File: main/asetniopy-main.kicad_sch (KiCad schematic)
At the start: 20 parts, among them J1 Conn_01x02, J2 Conn_01x02, J3 Conn_01x02, J4 Conn_01x02, J5 Conn_01x02, J6 Power/Reset, J7 BAT+, J8 BAT-, U1 ProMicro, U2 LSM6DSO

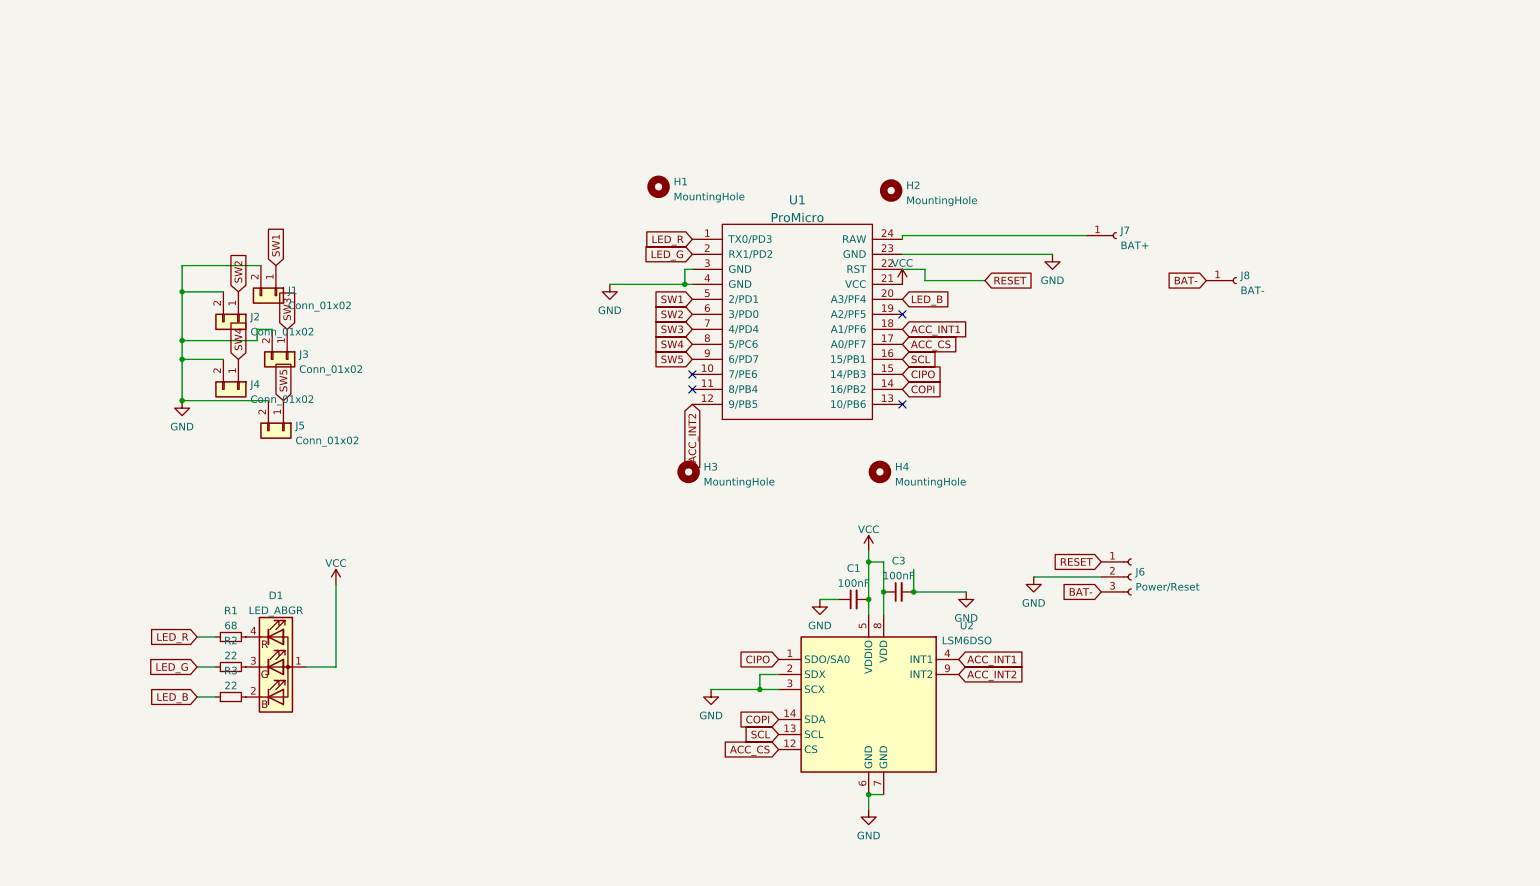
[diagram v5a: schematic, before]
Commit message: Left and right boards, joined via mouse bites.
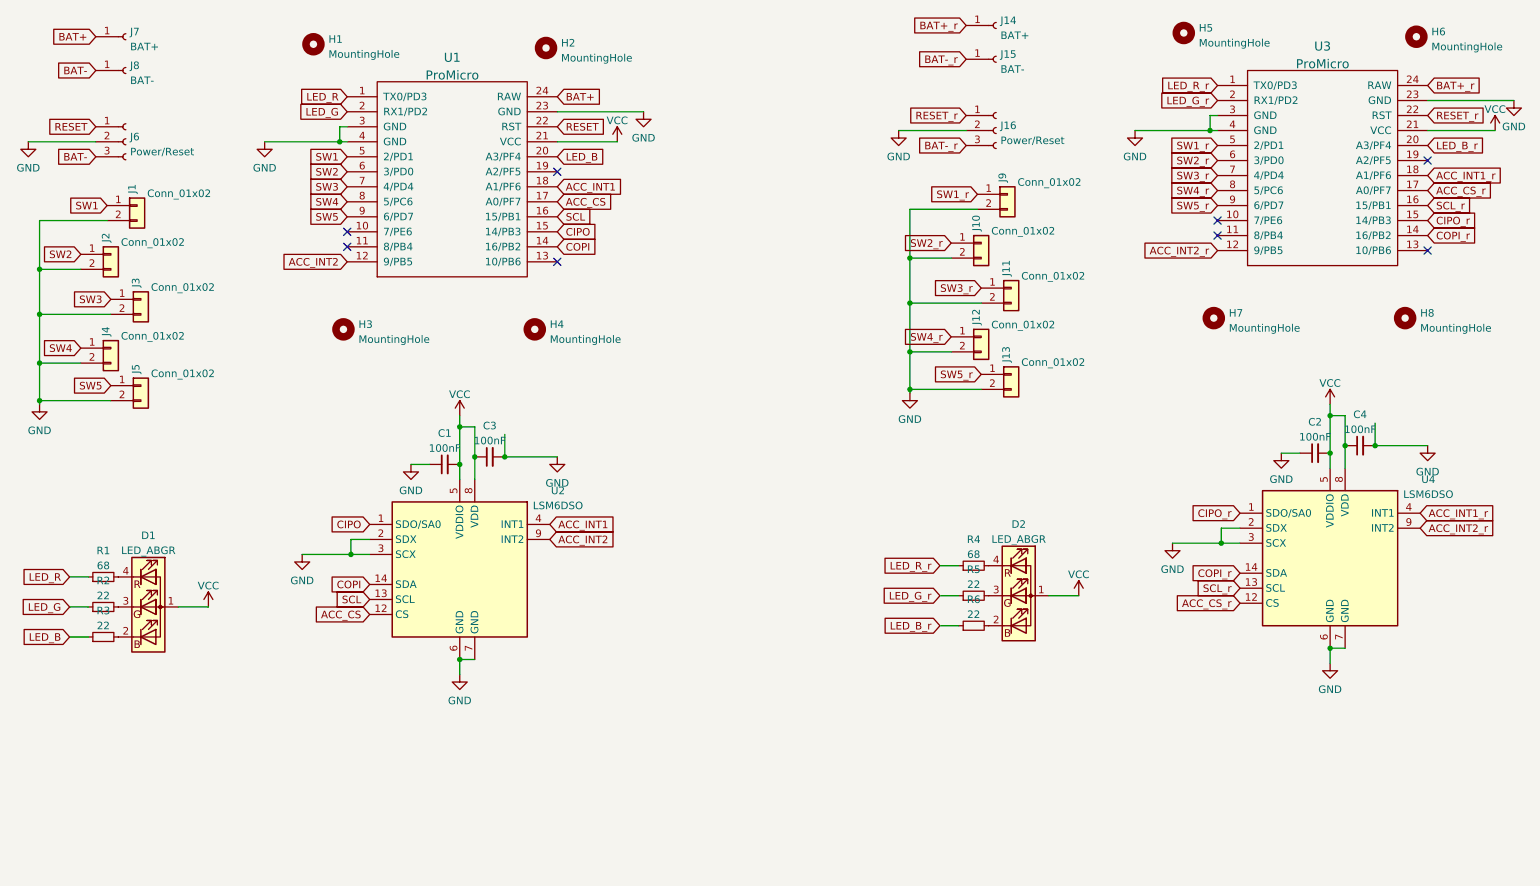
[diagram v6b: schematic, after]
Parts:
- added C2, C4: 100nF, Capacitor_SMD:C_0603_1608Metric, symbol Device:C_Small
- added D2: LED_ABGR, LED_SMD:LED_RGB_Wuerth-PLCC4_3.2x2.8mm_150141M173100, symbol Device:LED_ABGR
- added H5, H6, H7, H8: MountingHole, MountingHole:MountingHole_2.2mm_M2_Pad, symbol Mechanical:MountingHole
- added J10, J11, J12, J13, J9: Conn_01x02, Connector_Molex:Molex_Pico-EZmate_78171-0002_1x02-1MP_P1.20mm_Vertical, symbol Connector_Generic:Conn_01x02
- added J14: BAT+, Connector_PinSocket_2.54mm:PinSocket_1x01_P2.54mm_Vertical, symbol Connector:Conn_01x01_Female
- added J15: BAT-, Connector_PinSocket_2.54mm:PinSocket_1x01_P2.54mm_Vertical, symbol Connector:Conn_01x01_Female
- added J16: Power/Reset, Connector_Molex:Molex_Pico-EZmate_78171-0003_1x03-1MP_P1.20mm_Vertical, symbol Connector:Conn_01x03_Female
- added R4: 68, Resistor_SMD:R_0603_1608Metric, symbol Device:R_Small
- added R5, R6: 22, Resistor_SMD:R_0603_1608Metric, symbol Device:R_Small
- added U3: ProMicro, Keebio-Parts:ArduinoProMicro, symbol keebio:ProMicro
- added U4: LSM6DSO, main:PQFN50P250X300X86-14N, symbol Sensor_Motion:LSM6DS3
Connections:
- net BAT+: now reaches J7.1 (Pin_1), U1.24 (RAW)
- new net: D2.3 (GK), R5.2
- new net: D2.4 (RK), R4.2
- new net: D2.2 (BK), R6.2
- new net ACC_CS_r: U3.17 (A0/PF7), U4.12 (CS)
- new net ACC_INT1_r: U3.18 (A1/PF6), U4.4 (INT1)
- new net ACC_INT2_r: U3.12 (9/PB5), U4.9 (INT2)
- new net BAT+_r: J14.1 (Pin_1), U3.24 (RAW)
- new net BAT-_r: J15.1 (Pin_1), J16.3 (Pin_3)
- new net CIPO_r: U3.15 (14/PB3), U4.1 (SDO/SA0)
- new net COPI_r: U3.14 (16/PB2), U4.14 (SDA)
- new net GND1: C2.1, C4.2, J10.2 (Pin_2), J11.2 (Pin_2), J12.2 (Pin_2), J13.2 (Pin_2), J16.2 (Pin_2), J9.2 (Pin_2), U3.23 (GND), U3.3 (GND), U3.4 (GND), U4.2 (SDX), U4.3 (SCX), U4.6 (GND), U4.7 (GND)
- new net LED_B_r: R6.1, U3.20 (A3/PF4)
- new net LED_G_r: R5.1, U3.2 (RX1/PD2)
- new net LED_R_r: R4.1, U3.1 (TX0/PD3)
- new net RESET_r: J16.1 (Pin_1), U3.22 (RST)
- new net SCL_r: U3.16 (15/PB1), U4.13 (SCL)
- new net SW1_r: J9.1 (Pin_1), U3.5 (2/PD1)
- new net SW2_r: J10.1 (Pin_1), U3.6 (3/PD0)
- new net SW3_r: J11.1 (Pin_1), U3.7 (4/PD4)
- new net SW4_r: J12.1 (Pin_1), U3.8 (5/PC6)
- new net SW5_r: J13.1 (Pin_1), U3.9 (6/PD7)
- new net VCCQ: C2.2, C4.1, D2.1 (A), U3.21 (VCC), U4.5 (VDDIO), U4.8 (VDD)
- no-connect marks 4 -> 8
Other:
- moved on the sheet: C1, C3, D1, H1, H2, H3, H4, J1, J2, J3, J4, J5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

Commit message: Add part number for gyro.
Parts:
- U2, U4: LCSC Part Number (none) -> C2655100
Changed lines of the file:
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@@
+      (effects (font (size 1.27 1.27)) hide)
+    )
+    (property "LCSC Part Number" "C2655100" (id 4) (at 244.475 116.205 0)
       (effects (font (size 1.27 1.27)) hide)
     )
@@
       (effects (font (size 1.27 1.27)) hide)
     )
+    (property "LCSC Part Number" "C2655100" (id 4) (at 97.155 118.11 0)
+      (effects (font (size 1.27 1.27)) hide)
+    )

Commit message: Proper 0603 resistors.
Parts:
- R2, R3, R5, R6: LCSC Part Number C25092 -> C23345
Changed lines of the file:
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@@
       (effects (font (size 1.27 1.27)) hide)
     )
-    (property "LCSC Part Number" "C25092" (id 4) (at 36.83 129.54 90)
+    (property "LCSC Part Number" "C23345" (id 4) (at 36.83 129.54 90)
       (effects (font (size 1.27 1.27)) hide)
     )
@@
       (effects (font (size 1.27 1.27)) hide)
     )
-    (property "LCSC Part Number" "C25092" (id 4) (at 184.15 122.555 90)
+    (property "LCSC Part Number" "C23345" (id 4) (at 184.15 122.555 90)
       (effects (font (size 1.27 1.27)) hide)
     )
@@
       (effects (font (size 1.27 1.27)) hide)
     )
-    (property "LCSC Part Number" "C25092" (id 4) (at 184.15 127.635 90)
+    (property "LCSC Part Number" "C23345" (id 4) (at 184.15 127.635 90)
       (effects (font (size 1.27 1.27)) hide)
     )
@@
       (effects (font (size 1.27 1.27)) hide)
     )
-    (property "LCSC Part Number" "C25092" (id 4) (at 36.83 124.46 90)
-      (effects (font (size 1.27 1.27)) hide)
-    )
+    (property "LCSC Part Number" "C23345" (id 4) (at 36.83 124.46 90)
+      (effects (font (size 1.27 1.27)) hide)
+    )
